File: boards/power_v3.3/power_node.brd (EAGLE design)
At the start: 80 x 51 mm, 31 parts, among them J1 AVR_SPI_PRG_6NS, J2 12146734, U1 ATtiny167, U2 MCP2025, U3 MC17XSF500

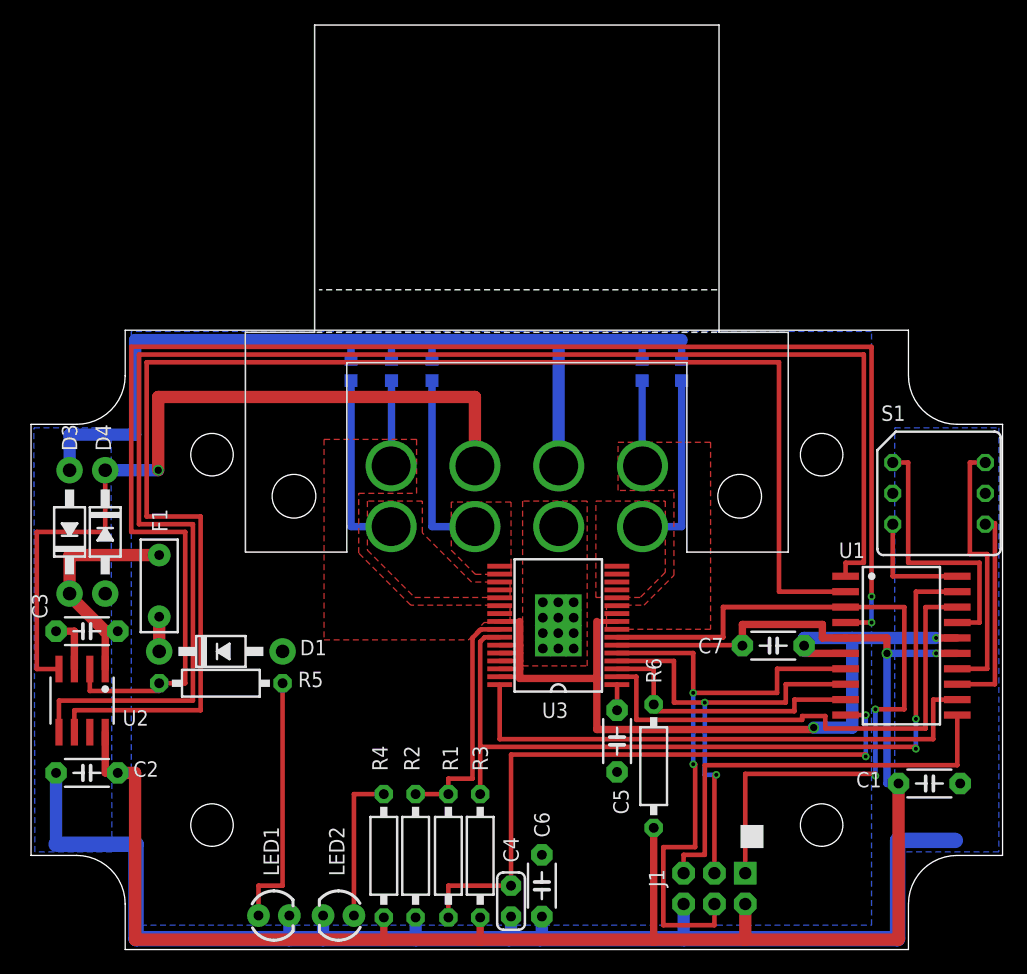
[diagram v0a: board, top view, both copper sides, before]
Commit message: Update to current sample boards
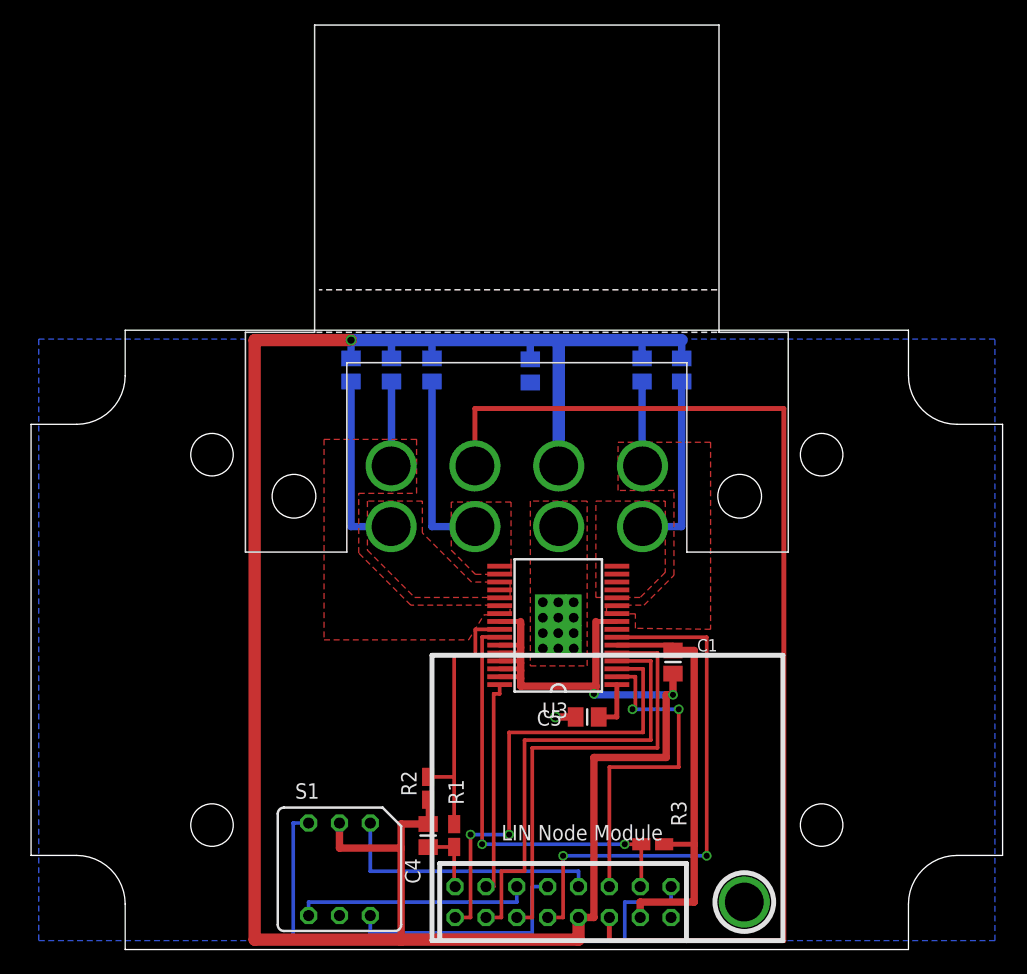
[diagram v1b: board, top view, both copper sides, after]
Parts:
- removed C2: 4u7, custom:C050-024X044
- removed C3: 22u, custom:C050-024X044
- removed C7: 0u1, custom:C050-024X044
- removed D1: 1N4004, custom:DO41-10
- removed D3, D4: P4KE30CA, custom:DO41-10
- removed F1: 10R / 300mA, custom:PTC
- removed J1: AVR_SPI_PRG_6NS, custom:2X3-NS
- removed LED1: RED, custom:LED3MM
- removed LED2: GREEN, custom:LED3MM
- removed R4, R5: 1K0, custom:0207/10
- removed R6: 4K99, custom:0207/10
- removed U1: ATtiny167, custom:SO20W
- removed U2: MCP2025, custom:SO08
- added U$2: (no value), custom:LIN_NODE
- C1, C5, C6: device custom:C050-024X044 -> custom:C0805K
- C10, C11, C12, C8, C9: device custom:C0603K -> custom:C0805K
- C4: device custom:C025-024X044 -> custom:C0805K
- R1, R2, R3: device custom:0207/10 -> custom:R0805W
- moved S1 58.3 mm to (33.0, 17.3), turned to 90 degrees
- moved C6 42.4 mm to (48.7, 58.3), flipped to the bottom, turned to 90 degrees
- moved C1 23.4 mm to (60.5, 34.4), turned to 270 degrees
- moved R3 14.2 mm to (58.8, 19.4), turned to 0 degrees
- moved C4 8.70 mm to (40.3, 20.1), turned to 90 degrees
- moved R2 5.65 mm to (40.3, 24.0)
- moved C5 3.16 mm to (53.4, 29.8), turned to 0 degrees
- moved R1 1.73 mm to (42.5, 20.1)
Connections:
- removed net !RESET: J1.5, U1.11
- removed net LINCS: R5.2, U1.4, U2.2
- removed net LINRX: U1.1, U2.5
- removed net LINTX: U1.2, U2.6
- removed net N$2: C3.1, D3.C, F1.P$1, U2.1
- removed net N$3: LED1.A, R5.1
- removed net N$4: LED2.A, R4.1
- removed net N$5: D1.C, F1.P$2
- net +12V: now also U$2.2; no longer D1.A
- net +5V: now also U$2.4; no longer C2.1, C7.1, J1.2, R4.2, R6.2, U1.15, U1.5, U2.8
- net CSNS: now also U$2.15; no longer U1.10
- net GND: now also U$2.8; no longer C2.2, C3.2, C7.2, D3.A, D4.A, J1.6, LED1.K, LED2.K, U1.16, U1.6, U2.3
- net ID1: now also U$2.7; no longer U1.17
- net ID2: now also U$2.11; no longer U1.13
- net ID4: now also U$2.1; no longer U1.20
- net ID8: now also U$2.9; no longer U1.14
- net LIN: now also U$2.6; no longer D4.C, U2.4
- net MISO: now also U$2.10; no longer J1.1, U1.3
- net MOSI: now also U$2.12; no longer J1.4, U1.7
- net SCK: now also U$2.14; no longer J1.3, U1.8
- net SWCLK: now also U$2.13; no longer U1.12
- net SWCS: now also U$2.16; no longer R6.1, U1.9
- net SWRSTB: now also U$2.5; no longer U1.18
- net SWSYNCB: now also U$2.3; no longer U1.19
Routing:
- net LINCS: track 128.2 -> 0.00 mm, vias 2 -> 0
- net LINRX: track 126.0 -> 0.00 mm
- net LINTX: track 121.7 -> 0.00 mm
- net +5V: track 154.9 -> 35.7 mm, vias 2 -> 0
- net GND: track 269.6 -> 219.2 mm, vias 2 -> 3
- net CSNS: track 53.0 -> 5.50 mm, vias 2 -> 0
- net ID4: track 9.60 -> 46.5 mm
- net !RESET: track 35.6 -> 0.00 mm
- net SWSYNCB: track 66.7 -> 35.2 mm
- net SWCLK: track 45.4 -> 17.8 mm
- net LIN: track 66.0 -> 90.2 mm, vias 1 -> 0
- net N$3: track 21.1 -> 0.00 mm
- net N$2: track 19.0 -> 0.00 mm
- net MISO: track 61.5 -> 43.6 mm
- net MOSI: track 52.0 -> 36.7 mm, vias 2 -> 0
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- removed copper zone on layer 16, net GND
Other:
- board text added: "LIN power node v3.3 (c)2014 michael smith"
- board text removed: "LIN power node v3.1 (c)2014 michael smith"
